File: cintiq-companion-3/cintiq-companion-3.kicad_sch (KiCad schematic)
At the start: 8 parts, among them J1 13HD_eDP, J2 13HD_penpanel, J3 13HD_buttonboard, J4 13HD_fingerpanel

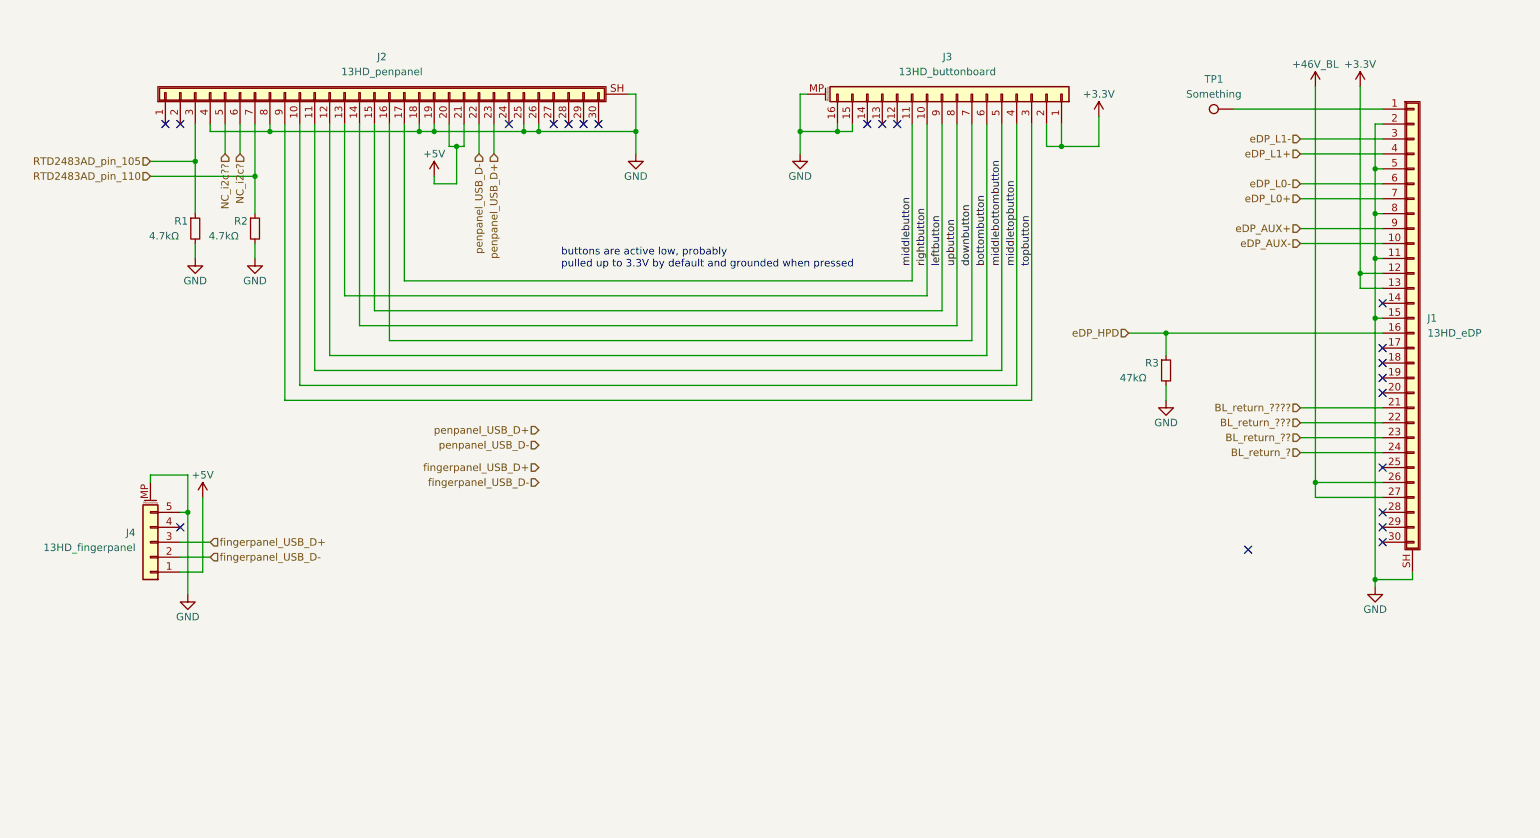
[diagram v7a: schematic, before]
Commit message: Changed 30-pin symbols to ipex
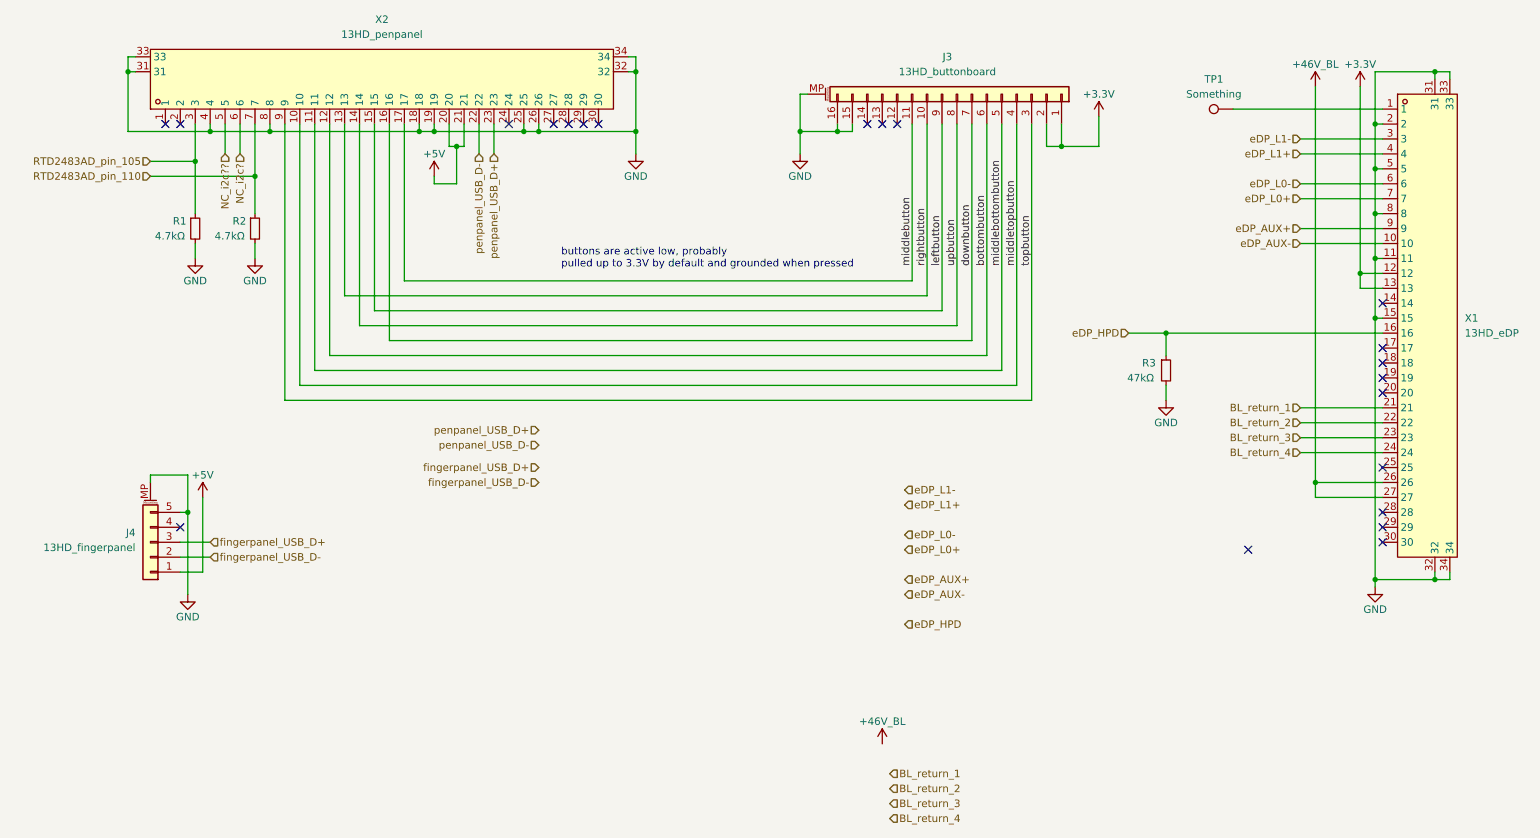
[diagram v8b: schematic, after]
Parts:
- removed J1: 13HD_eDP, symbol Connector_Generic_Shielded:Conn_01x30_Shielded
- removed J2: 13HD_penpanel, symbol Connector_Generic_Shielded:Conn_01x30_Shielded
- added X1: 13HD_eDP, 30pipex:FPC-SMD_ALC04-S30EIA-00, symbol A_my_stuff:30pipex
- added X2: 13HD_penpanel, 30pipex:FPC-SMD_ALC04-S30EIA-00, symbol A_my_stuff:30pipex
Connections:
- net +3.3V: now also X1.12, X1.13
- net +46V_BL: now also X1.26, X1.27
- net +5V: now also X2.20, X2.21
- net GND: now also X1.11, X1.15, X1.2, X1.31, X1.32, X1.33, X1.34, X1.5, X1.8, X2.18, X2.19, X2.25, X2.26, X2.31, X2.32, X2.33, X2.34, X2.4, X2.8
- net NC_i2c?: now also X2.6
- net NC_i2c??: now also X2.5
- net RTD2483AD_pin_105: now also X2.3
- net RTD2483AD_pin_110: now also X2.7
- net bottombutton: now also X2.12
- net downbutton: now also X2.16
- net eDP_AUX+: now also X1.9
- net eDP_AUX-: now also X1.10
- net eDP_HPD: now also X1.16
- net eDP_L0+: now also X1.7
- net eDP_L0-: now also X1.6
- net eDP_L1+: now also X1.4
- net eDP_L1-: now also X1.3
- net leftbutton: now also X2.15
- net middlebottombutton: now also X2.11
- net middlebutton: now also X2.17
- net middletopbutton: now also X2.10
- net penpanel_USB_D+: now also X2.23
- net penpanel_USB_D-: now also X2.22
- net rightbutton: now also X2.13
- net topbutton: now also X2.9
- net upbutton: now also X2.14
- net at TP1.1: now also X1.1
- new net BL_return_1: X1.21
- new net BL_return_2: X1.22
- new net BL_return_3: X1.23
- new net BL_return_4: X1.24
